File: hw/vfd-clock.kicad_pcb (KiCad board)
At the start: 2 copper layers, 150 x 50 mm, 47 parts, among them CON1 BARREL_JACK_2, CON2 BARREL_JACK_2, M1 MountingHole_4-5mm, M2 MountingHole_4-5mm, P1 ST_LINK, P2 GPS, Q1 PNP, Q2 PNP, SW1 SET, SW2 UP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

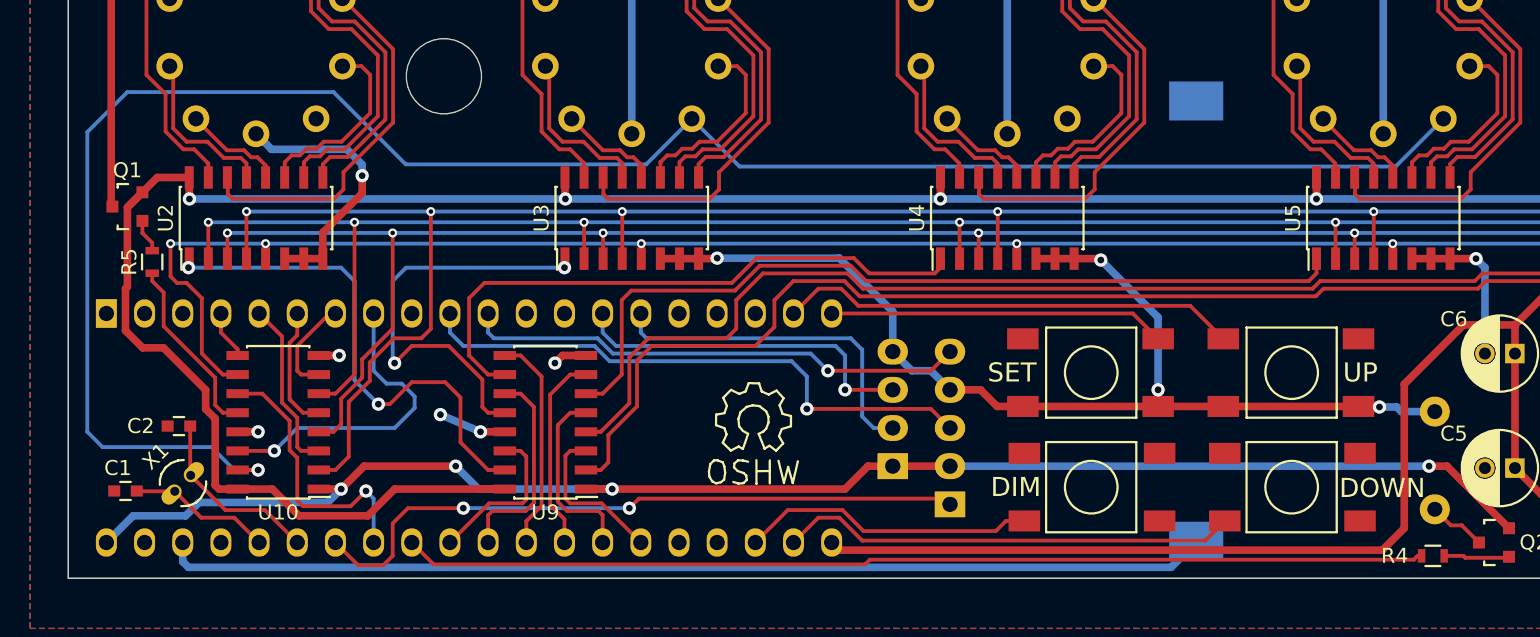
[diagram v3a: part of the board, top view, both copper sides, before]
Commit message: volt shifters ssop->tssop
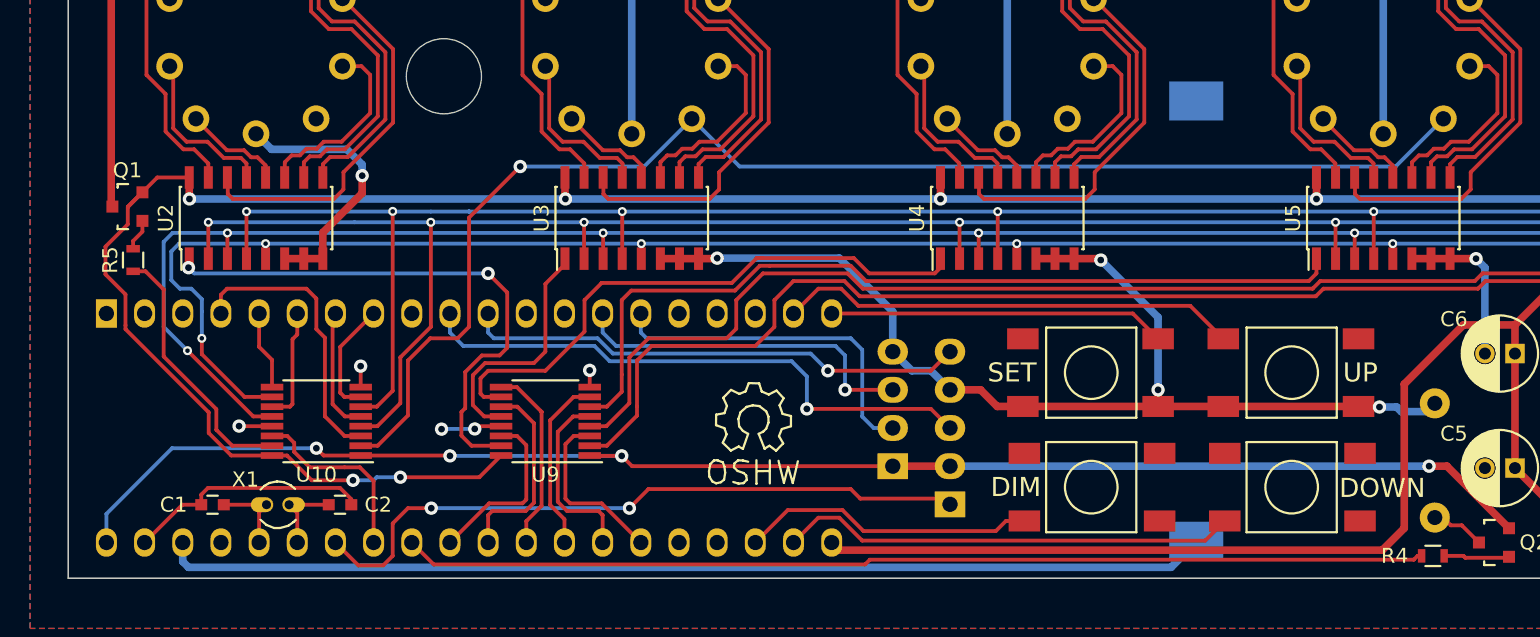
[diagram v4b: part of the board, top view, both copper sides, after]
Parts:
- SP1: footprint AT-1224-TWT -> Buzzers_Beepers:Buzzer_12x9.5RM7.6
- U10, U9: footprint Housings_SOIC:SOIC-16_3.9x9.9mm_Pitch1.27mm -> VFD:TSSOP-16_4.4x5mm_Pitch0.65mm
- moved C2 11.9 mm to (43.5, 70.5), turned to 0 degrees
- moved X1 6.48 mm to (39.3, 70.5), turned to 0 degrees
- moved C1 5.86 mm to (35.0, 70.5)
- moved U10 2.54 mm to (41.9, 65.0)
- moved R5 1.28 mm to (29.7, 54.2)
- moved U9 0.06 mm to (57.1, 65.0)
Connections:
- U1 pad 4: /DAL -> /DPL
- U1 pad 5: /DDL -> /DAL
- U1 pad 8: /DPL -> /DDL
- U10 pad 11: /GRIDL -> /DBL
- U10 pad 12: /GRIDH -> /DBH
- U10 pad 14: /DPL -> /GRIDL
- U10 pad 15: /DPH -> /GRIDH
- U10 pad 2: /DDH -> /DPH
- U10 pad 3: /DDL -> /DPL
- U10 pad 4: /DBH -> /DCH
- U10 pad 5: /DBL -> /DCL
- U10 pad 6: /DCH -> /DDH
- U10 pad 7: /DCL -> /DDL
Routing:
- net /DPH: track 130.9 -> 90.1 mm
- net /GND: track 163.4 -> 179.0 mm
- net /STROBE2H: track 28.6 -> 17.0 mm, vias 2 -> 0
- net /DDH: track 165.8 -> 158.4 mm
- net Net-(C2-Pad1): track 12.2 -> 5.38 mm
- net /GRIDL: track 18.5 -> 12.4 mm, vias 1 -> 0
- net /GRIDH: track 12.2 -> 17.5 mm
- net Net-(C1-Pad1): track 9.56 -> 5.56 mm
- net /DBH: track 151.1 -> 155.1 mm
- net /DDL: track 11.5 -> 7.67 mm
- net /DCH: track 152.9 -> 156.0 mm
- net /STROBE1H: track 34.1 -> 36.9 mm
- net /19v5: track 269.3 -> 266.5 mm, vias 6 -> 8
- net /DAH: track 148.8 -> 151.4 mm
- net /DAL: track 3.25 -> 5.26 mm
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
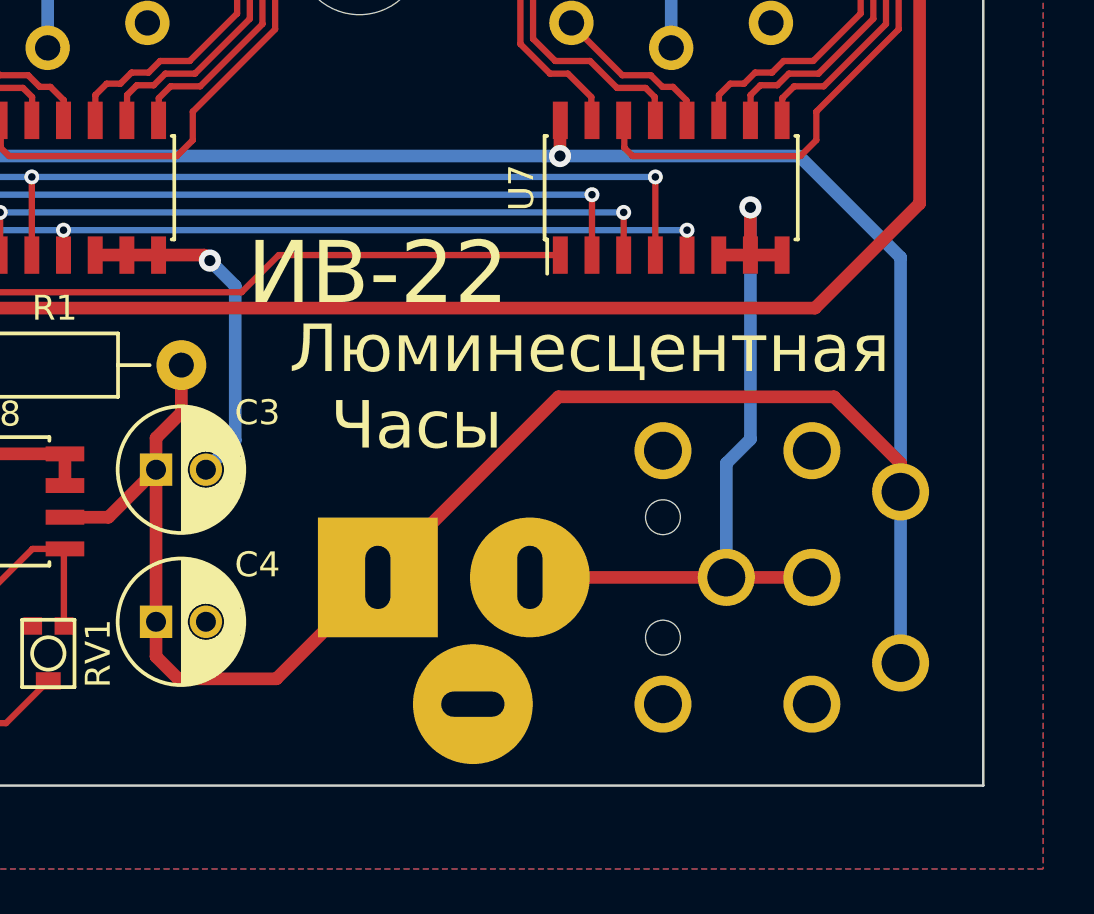
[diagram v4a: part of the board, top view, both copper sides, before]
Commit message: rotate power jacks for plug clearance
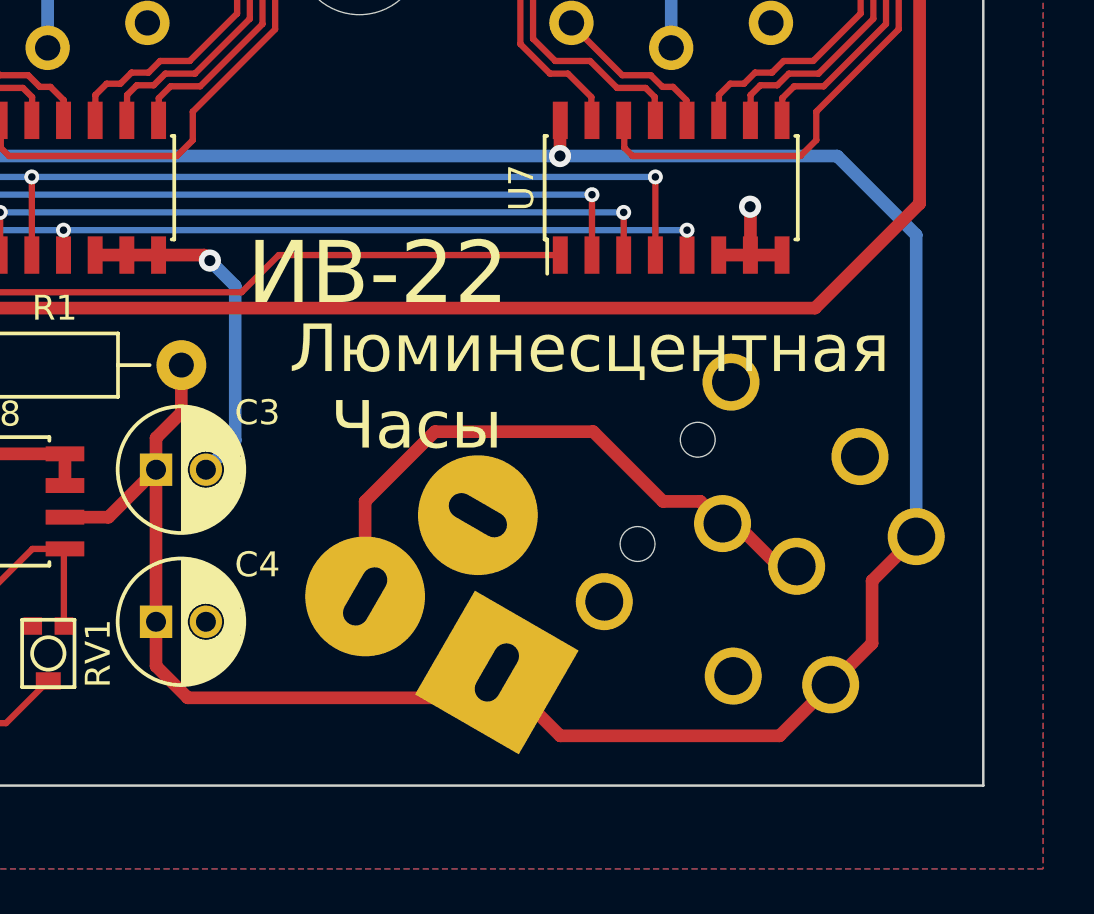
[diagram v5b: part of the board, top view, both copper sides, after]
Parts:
- moved CON1 6.65 mm to (150.6, 67.8), turned to 330 degrees
- moved CON2 1.80 mm to (165.6, 65.3), turned to 330 degrees
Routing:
- net /19v5: track 266.5 -> 261.7 mm
- net /GND: track 179.0 -> 177.0 mm

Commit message: Add README, LICENSE, github link.
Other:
- board text added: "https://github.com/arantius/vfd-clock"
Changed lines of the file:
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@@
     (area 25.349999 25.349999 175.450001 75.450001)
     (thickness 1.6)
-    (drawings 11)
+    (drawings 12)
     (tracks 1067)
     (zones 0)
@@
     )
   )
+  (gr_text https://github.com/arantius/vfd-clock (at 55.118 48.8315) (layer B.SilkS)
+    (effects (font (size 1.5 1.5) (thickness 0.3)) (justify mirror))
+  )
   (gr_text DIM (at 88.4555 69.342) (layer F.SilkS)
